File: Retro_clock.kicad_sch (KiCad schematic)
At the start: 33 parts, among them J1 Conn_01x08_Female, J2 Conn_01x08_Female, J3 Conn_01x10_Female, SW1 Rotary_Encoder_Switch, SW2 KLS7-TS6601-13.0-180, SW3 KLS7-TS6601-13.0-180, U1 K155ID1, U2 K155ID1, U3 K155ID1, U4 K155ID1

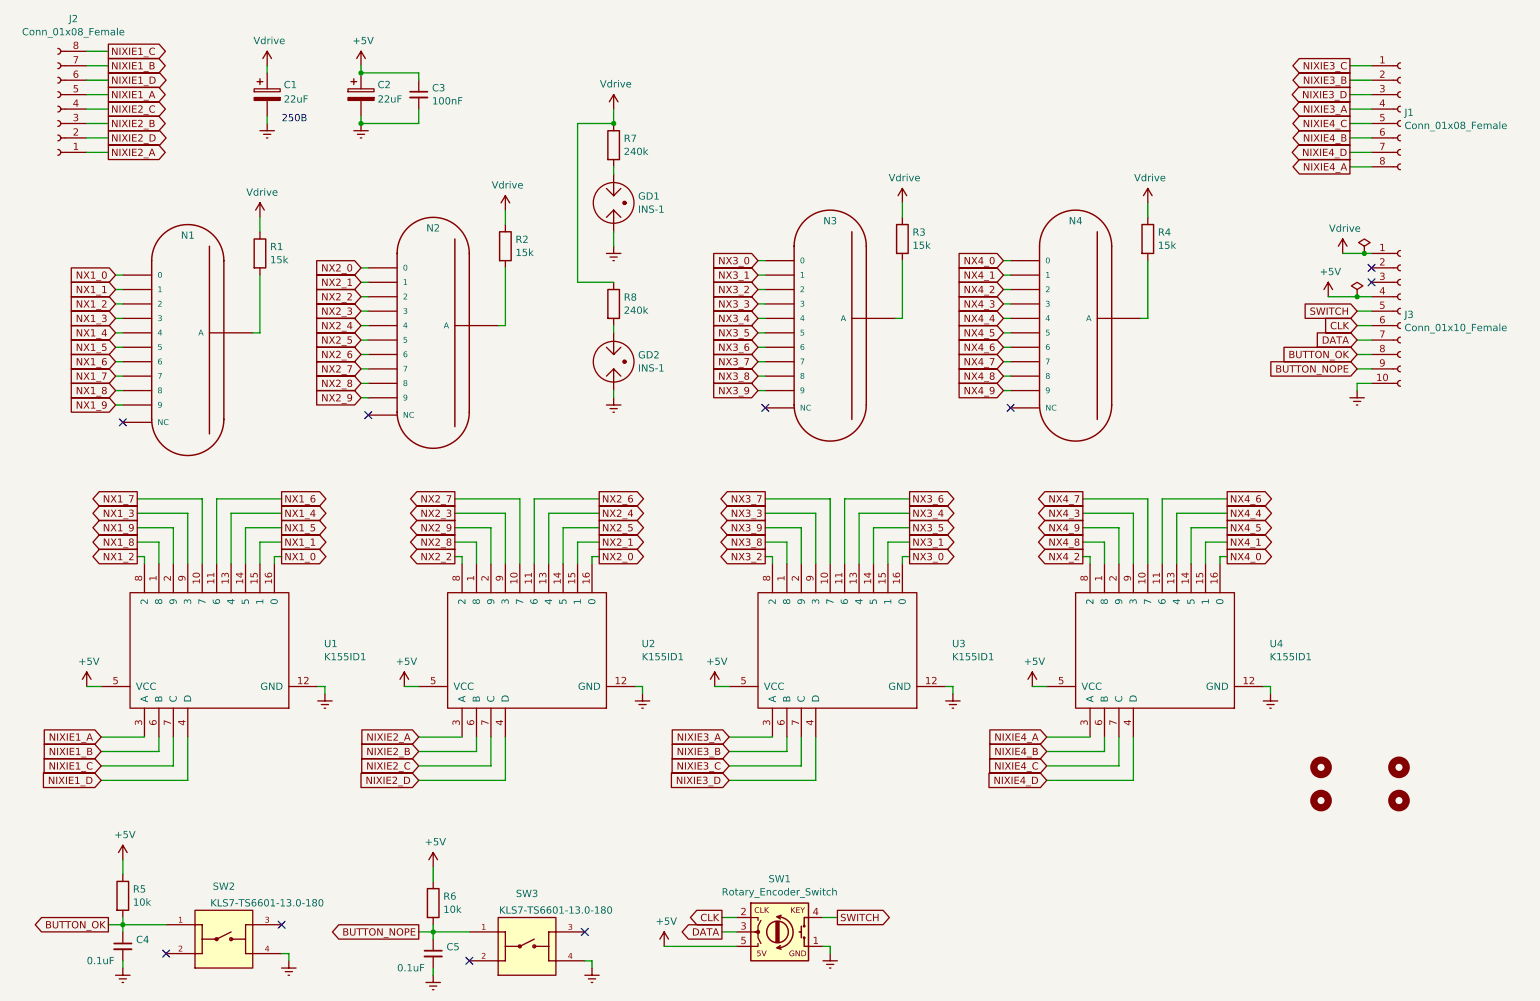
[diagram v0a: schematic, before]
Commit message: Finished first pcb, 2nd schematics and footprints.
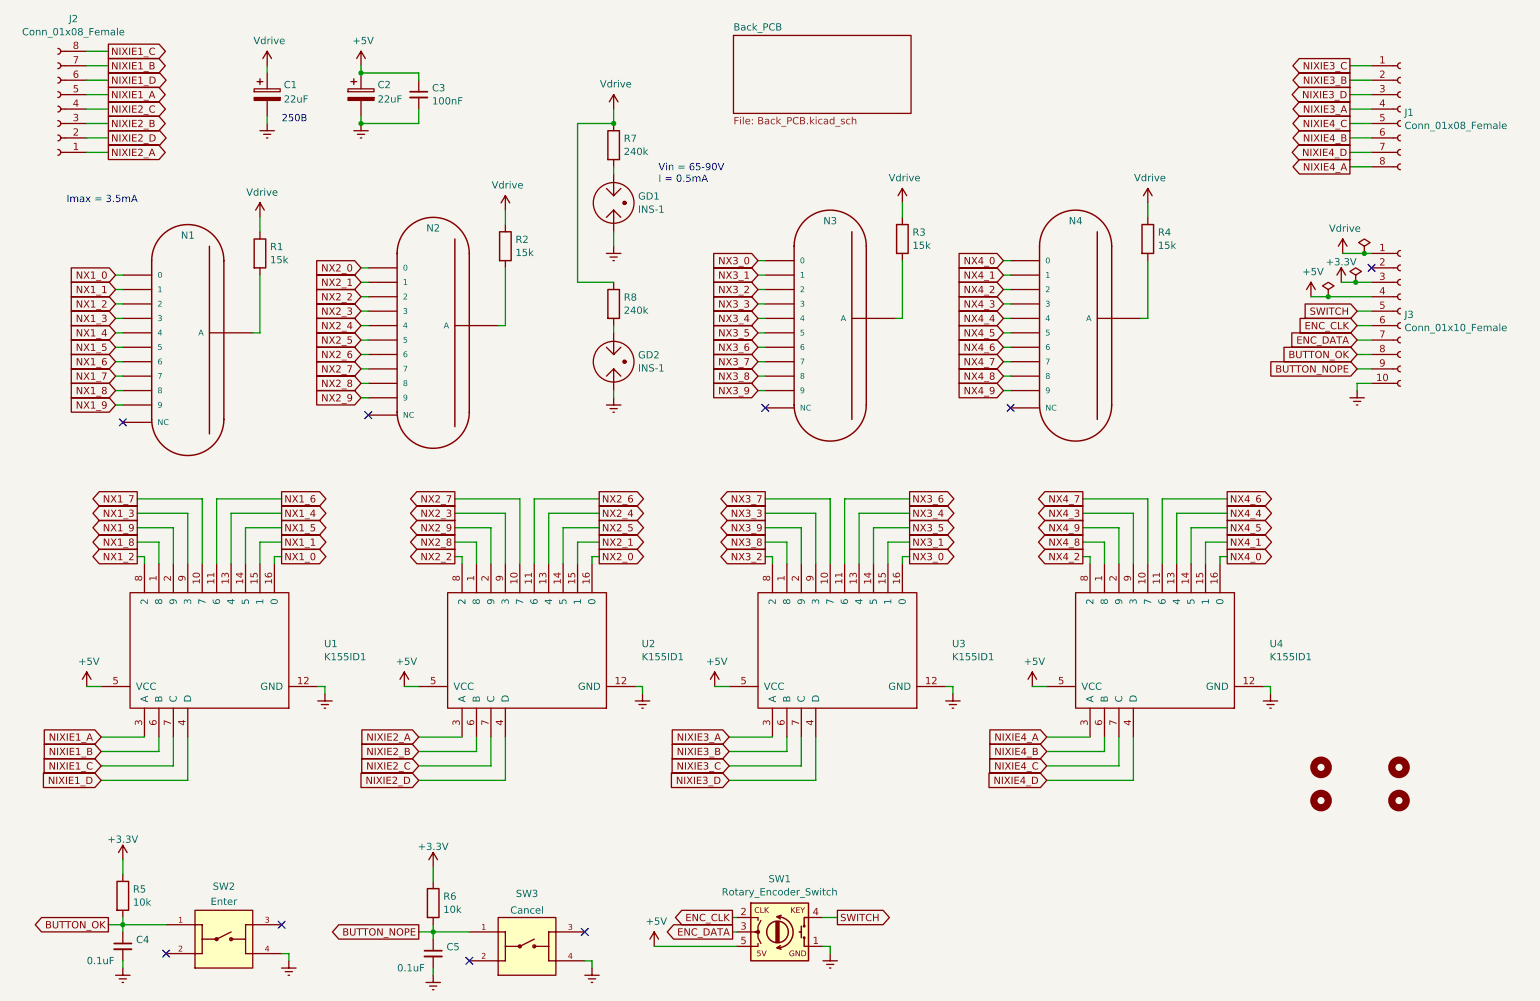
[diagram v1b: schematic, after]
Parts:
- C2: footprint Capacitor_Tantalum_SMD:CP_EIA-7361-38_AVX-V_Pad2.18x3.30mm_HandSolder -> Capacitor_Tantalum_SMD:CP_EIA-3216-10_Kemet-I_Pad1.58x1.35mm_HandSolder
- SW2: value KLS7-TS6601-13.0-180 -> Enter
- SW3: value KLS7-TS6601-13.0-180 -> Cancel
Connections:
- net +5V: no longer R5.1, R6.1
- net +3.3V: now reaches J3.3 (Pin_3)
- net +3.3V: now also R5.1, R6.1
- net CLK renamed ENC_CLK
- net DATA renamed ENC_DATA
- no-connect marks 10 -> 9
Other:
- added sheet Back_PCB (Back_PCB.kicad_sch)
- note added: "Imax = 3.5mA"
- note added: "Vin = 65-90V I = 0.5mA"

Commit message: Final version without panelization.
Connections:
- net +3.3V: now also J3.4 (Pin_4); no longer J3.3 (Pin_3)
- net +5V: now also J3.3 (Pin_3); no longer J3.4 (Pin_4)
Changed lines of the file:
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@@
     (pin "1")
   )
-  (symbol (lib_id "power:+5V") (at 243.332 63.5 0) (unit 1)
-    (in_bom yes) (on_board yes)
-    (property "Reference" "#PWR014" (id 0) (at 243.332 67.31 0)
-      (effects (font (size 1.27 1.27)) hide)
-    )
-    (property "Value" "+5V" (id 1) (at 243.713 59.1058 0))
-    (property "Footprint" "" (id 2) (at 243.332 63.5 0)
-      (effects (font (size 1.27 1.27)) hide)
-    )
-    (property "Datasheet" "" (id 3) (at 243.332 63.5 0)
+  (symbol (lib_id "power:+5V") (at 248.666 60.96 0) (unit 1)
+    (in_bom yes) (on_board yes)
+    (property "Reference" "#PWR014" (id 0) (at 248.666 64.77 0)
+      (effects (font (size 1.27 1.27)) hide)
+    )
+    (property "Value" "+5V" (id 1) (at 248.0564 57.404 0))
+    (property "Footprint" "" (id 2) (at 248.666 60.96 0)
+      (effects (font (size 1.27 1.27)) hide)
+    )
+    (property "Datasheet" "" (id 3) (at 248.666 60.96 0)
       (effects (font (size 1.27 1.27)) hide)
     )
@@
     (pin "1")
   )
-  (symbol (lib_id "power:+3.3V") (at 248.666 60.96 0) (unit 1)
+  (symbol (lib_id "power:+3.3V") (at 243.332 63.5 0) (unit 1)
     (in_bom yes) (on_board yes) (fields_autoplaced)
-    (property "Reference" "#PWR016" (id 0) (at 248.666 64.77 0)
-      (effects (font (size 1.27 1.27)) hide)
-    )
-    (property "Value" "+3.3V" (id 1) (at 248.666 57.3842 0))
-    (property "Footprint" "" (id 2) (at 248.666 60.96 0)
-      (effects (font (size 1.27 1.27)) hide)
-    )
-    (property "Datasheet" "" (id 3) (at 248.666 60.96 0)
+    (property "Reference" "#PWR016" (id 0) (at 243.332 67.31 0)
+      (effects (font (size 1.27 1.27)) hide)
+    )
+    (property "Value" "+3.3V" (id 1) (at 243.332 59.9242 0))
+    (property "Footprint" "" (id 2) (at 243.332 63.5 0)
+      (effects (font (size 1.27 1.27)) hide)
+    )
+    (property "Datasheet" "" (id 3) (at 243.332 63.5 0)
       (effects (font (size 1.27 1.27)) hide)
     )
@@
       (reference "#PWR031") (unit 1) (value "+5VP") (footprint "")
     )
-    (path "/ad44c88a-2183-449f-9759-8c21b89dddd9/2aa2e24b-5718-4cc8-9429-990d68ddfb90"
-      (reference "#PWR032") (unit 1) (value "+3.3V") (footprint "")
+    (path "/ad44c88a-2183-449f-9759-8c21b89dddd9/4216fe1c-aea5-48e8-b133-39c6f39ff4bf"
+      (reference "#PWR032") (unit 1) (value "+3.3VP") (footprint "")
     )
     (path "/ad44c88a-2183-449f-9759-8c21b89dddd9/f7cdc0a3-7a41-48bc-940a-82b88aec3cd9"
@@
       (reference "#PWR071") (unit 1) (value "+5VP") (footprint "")
     )
+    (path "/ad44c88a-2183-449f-9759-8c21b89dddd9/1fc59174-21c3-4eeb-be87-b239c142cbf0"
+      (reference "#PWR072") (unit 1) (value "GND") (footprint "")
+    )
     (path "/ad44c88a-2183-449f-9759-8c21b89dddd9/538daafa-30b9-4504-8009-9392e83f95e7"
       (reference "#PWR0103") (unit 1) (value "+3.3VP") (footprint "")
@@
     )
     (path "/ad44c88a-2183-449f-9759-8c21b89dddd9/b8f2e657-2328-461e-8e8b-de9ad5cf279e/2ae737ac-4018-41ec-bc09-94e90ca4a7aa"
-      (reference "U10") (unit 1) (value "DD05CVSA") (footprint "Retro_clock:DD05CVSA")
+      (reference "U10") (unit 1) (value "DD04CVSA") (footprint "Retro_clock:DD04CVSA")
     )
     (path "/ad44c88a-2183-449f-9759-8c21b89dddd9/b8f2e657-2328-461e-8e8b-de9ad5cf279e/45f2bd1e-9cc9-4e9f-b1a7-7a02e547d192"
